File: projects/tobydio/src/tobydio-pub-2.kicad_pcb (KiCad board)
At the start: 2 copper layers, 42.3 x 41 mm, 41 parts, among them J1 Conn_01x02_Pin, J10 Conn_01x03_Pin, J2 PJ-320D-A, J3 Conn_01x04_Pin, J5 Conn_01x01_Pin, J6 Conn_01x03_Pin, J7 Conn_01x04_Pin, J8 PJ-320D-A, J9 Conn_01x03_Pin, U1 PCM5100APWR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

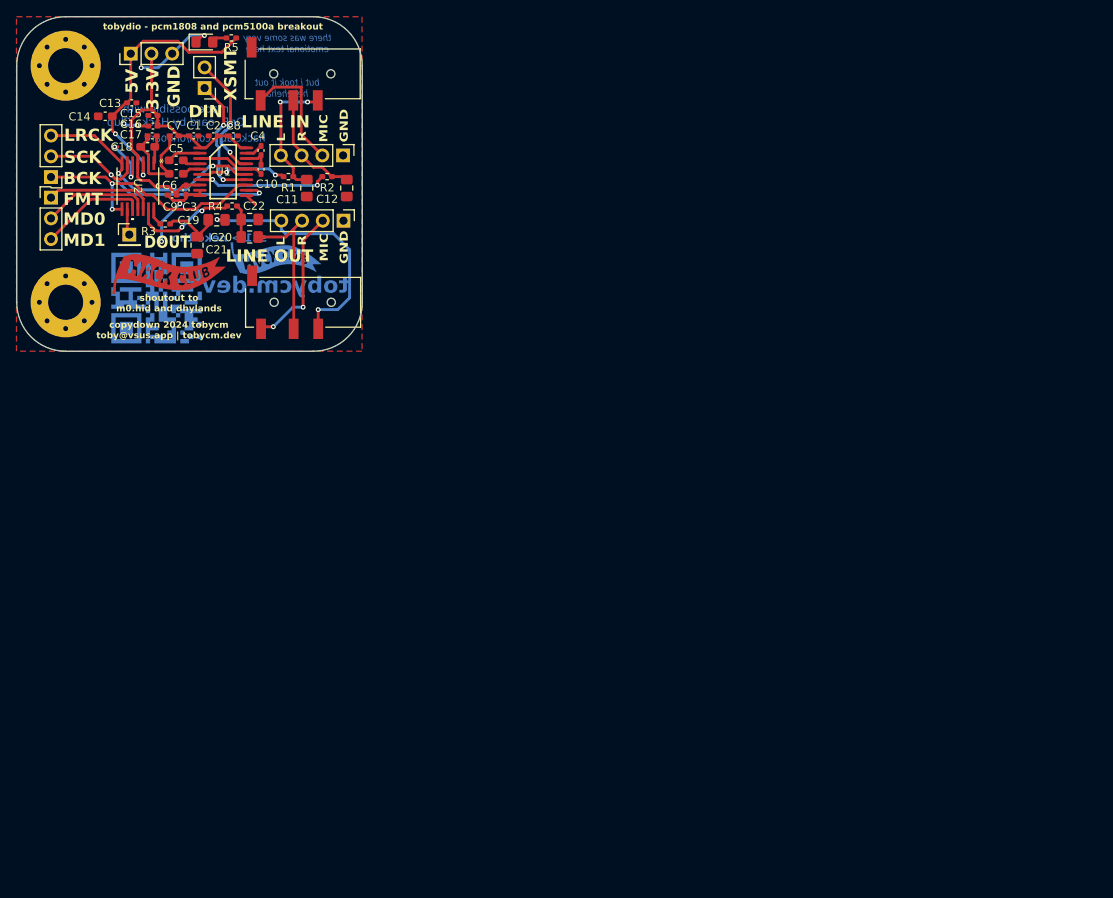
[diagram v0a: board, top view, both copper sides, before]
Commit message: update tobydio board errors
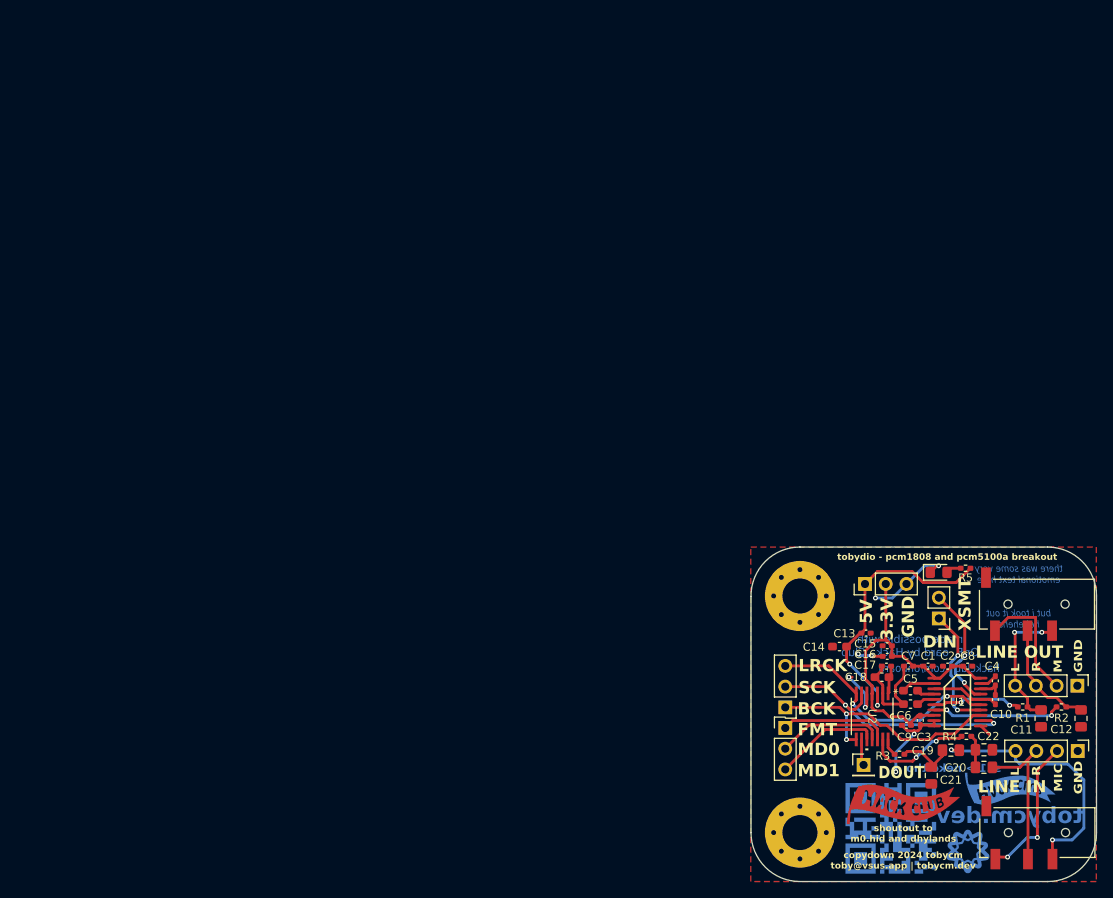
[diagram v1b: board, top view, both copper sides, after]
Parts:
- moved C2 111.0 mm to (128.3, 94.6)
- moved C1 111.0 mm to (125.9, 94.6)
- moved C10 111.0 mm to (134.2, 98.7)
- moved C11 111.0 mm to (139.8, 101.0)
- moved C12 111.0 mm to (144.7, 101.0)
- moved C13 111.0 mm to (118.3, 90.5)
- moved C14 111.0 mm to (115.0, 92.2)
- moved C15 111.0 mm to (120.9, 92.1)
- moved C16 111.0 mm to (120.9, 93.4)
- moved C17 111.0 mm to (120.8, 94.6)
- moved C18 111.0 mm to (120.2, 96.0)
- moved C19 111.0 mm to (128.7, 104.9)
- moved C20 111.0 mm to (132.8, 107.0)
- moved C21 111.0 mm to (126.3, 108.0)
- moved C22 111.0 mm to (132.8, 104.8)
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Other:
- board size 42.3 x 41 mm -> 42.4 x 41 mm
- board text added: "M"
